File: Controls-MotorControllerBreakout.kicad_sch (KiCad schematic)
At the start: 16 parts, among them J1 MC CAN 1, J2 MC CAN 2, J3 CTRLS, J4 EXT PWR, J5 CANDAPTER, J6 FAN 1, J7 FAN 2

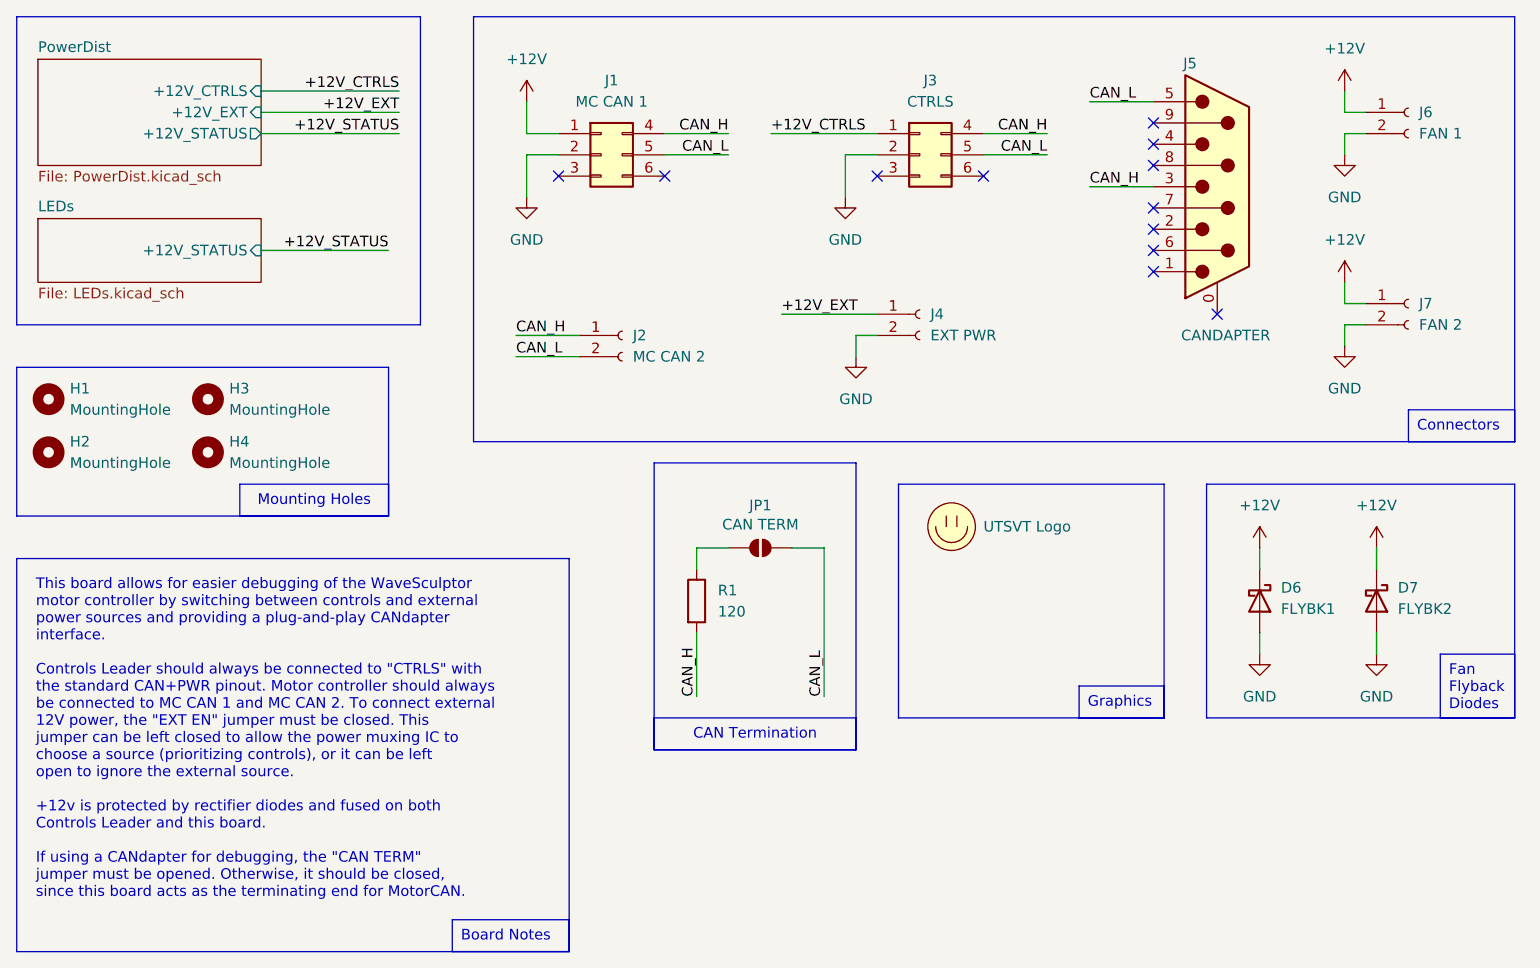
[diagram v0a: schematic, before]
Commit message: modify for PEAK candapter
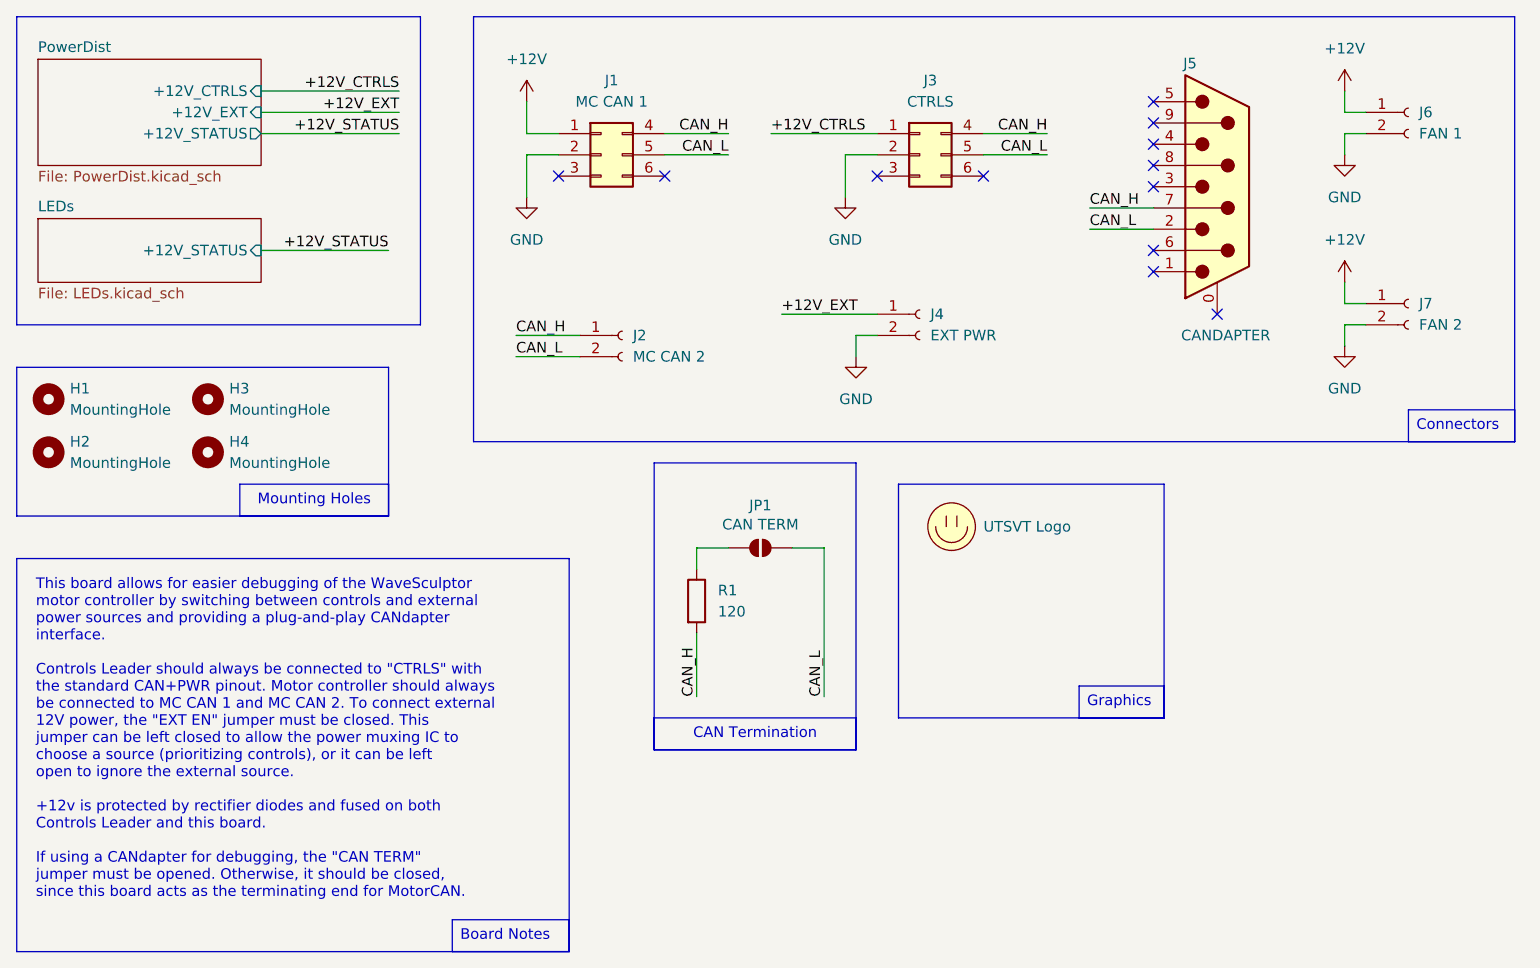
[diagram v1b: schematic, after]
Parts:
- removed D6: FLYBK1, UTSVT_Passive:DO-221AC, symbol Device:D_Schottky
- removed D7: FLYBK2, UTSVT_Passive:DO-221AC, symbol Device:D_Schottky
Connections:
- net CAN_H: now also J5.7; no longer J5.3
- net CAN_L: now also J5.2; no longer J5.5
